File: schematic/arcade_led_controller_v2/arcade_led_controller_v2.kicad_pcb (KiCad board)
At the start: 2 copper layers, 104.1 x 70 mm, 930 parts, among them P1_BALLTOP_LED_1 WS2812B, P1_BUTTONS_LED1 WS2812B, P1_DP_JOY_MODE_LED1 LED, P1_JOYSTICK_LED1 WS2812B, P1_LS_JOY_MODE_LED1 LED, P1_RS_JOY_MODE_LED1 LED, P2_BALLTOP_LED_1 WS2812B, P2_BUTTONS_LED1 WS2812B, P2_DP_JOY_MODE_LED1 LED, P2_JOYSTICK_LED1 WS2812B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

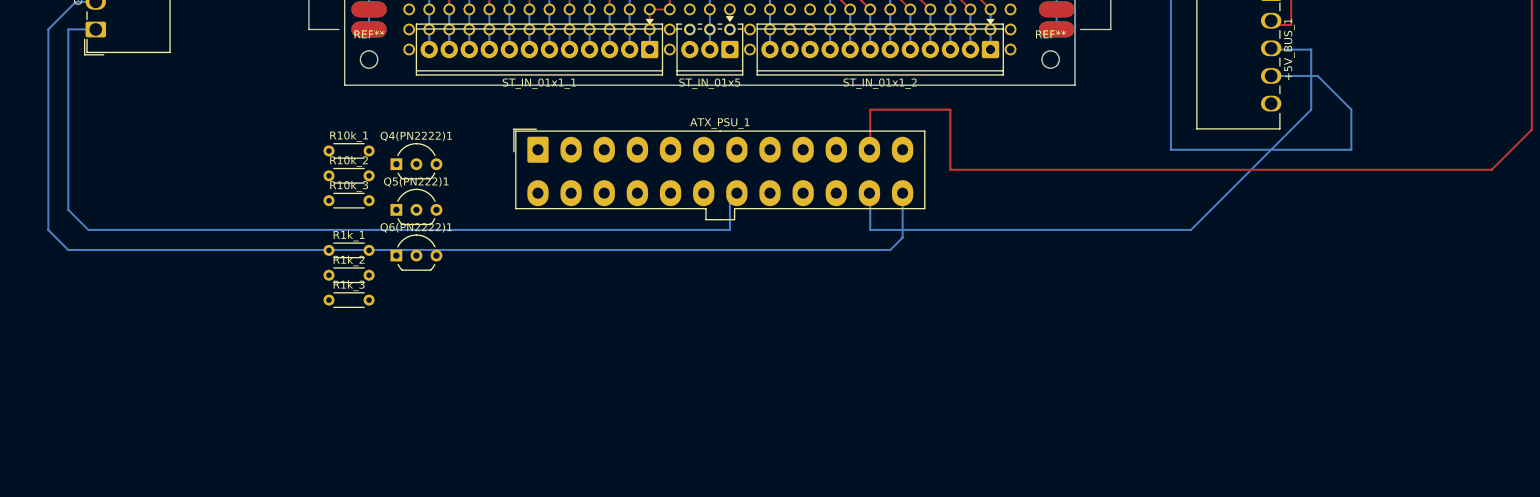
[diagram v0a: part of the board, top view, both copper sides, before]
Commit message: Update input pin assignments
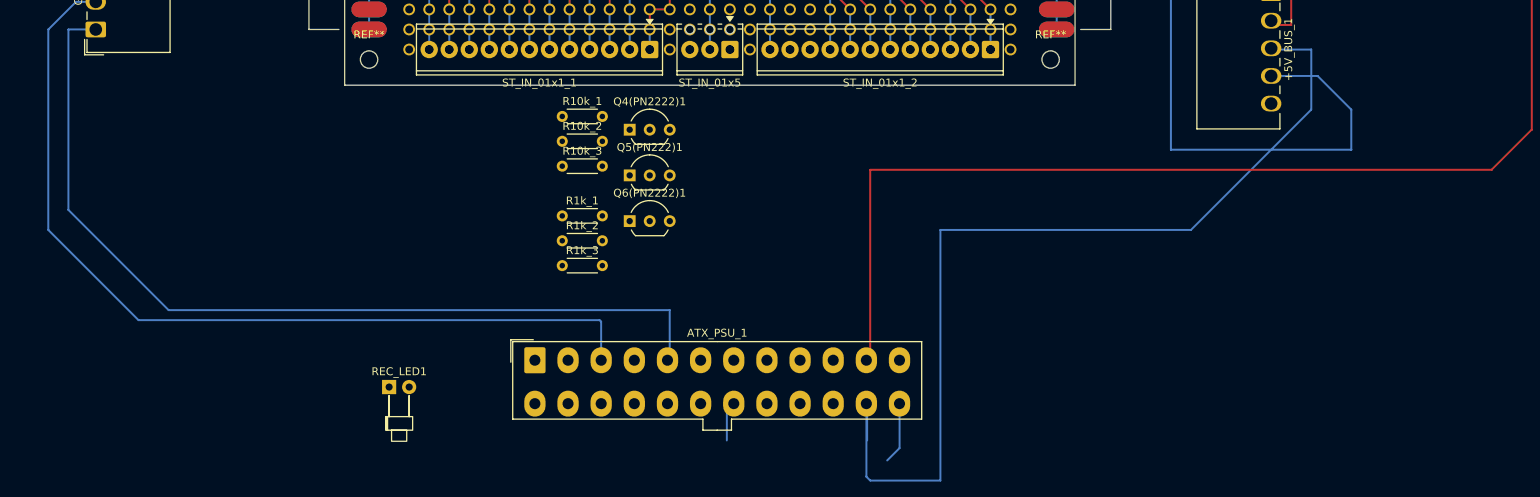
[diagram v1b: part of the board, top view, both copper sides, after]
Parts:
- added REC_LED1: LED, LED_THT:LED_D1.8mm_W1.8mm_H2.4mm_Horizontal_O3.81mm_Z1.6mm, F.Cu at (111.8, 174.8)
- moved Q4(PN2222)1 29.9 mm to (142.2, 142.2)
- moved Q5(PN222)1 29.9 mm to (142.2, 148.0)
- moved Q6(PN2222)1 29.9 mm to (142.2, 153.8)
- moved R10k_1 29.9 mm to (133.7, 140.6)
- moved R10k_2 29.9 mm to (133.7, 143.7)
- moved R1k_1 29.9 mm to (133.7, 153.2)
- moved R1k_2 29.9 mm to (133.7, 156.3)
- moved R1k_3 29.9 mm to (133.7, 159.5)
- moved R10k_3 29.9 mm to (133.7, 146.9)
- moved ATX_PSU_1 26.7 mm to (130.2, 171.4)
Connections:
- net /REC_LED renamed /REC_LED_CATHODE
- net Net-(Q4(PN2222)1-B) renamed /P2_LS_BASE_TO_GP
- net Net-(Q7(PN2222)1-B) renamed /REC_LED_BASE_TO_GP
- A1 pad 15: /ROTARY_SW -> Net-(A1-GPIO11)
- A1 pad 16: /ROTARY_DT -> /ROTARY_SW
- A1 pad 17: /P1_SIG -> /ROTARY_DT
- A1 pad 2: /P2_SIG -> /P1_SIG
- A1 pad 7: Net-(A1-GPIO5) -> /P2_SIG
- Q5(PN222)1 pad 2: Net-(Q5(PN222)1-B) -> GND
- Q6(PN2222)1 pad 2: Net-(Q6(PN2222)1-B) -> /P2_RS_BASE_TO_GP
- R10k_2 pad 1: Net-(Q5(PN222)1-B) -> GND
- R10k_3 pad 1: GND -> /P2_RS_BASE_TO_GP
- R10k_3 pad 2: Net-(Q6(PN2222)1-B) -> GND
- R1k_1 pad 1: Net-(A1-GPIO6) -> Net-(A1-GPIO8)
- R1k_2 pad 1: Net-(A1-GPIO8) -> Net-(A1-GPIO10)
- R1k_2 pad 2: Net-(Q5(PN222)1-B) -> GND
- R1k_3 pad 1: Net-(A1-GPIO10) -> Net-(A1-GPIO11)
- R1k_3 pad 2: Net-(Q6(PN2222)1-B) -> /P2_RS_BASE_TO_GP
- R1k_4 pad 1: Net-(A1-GPIO5) -> Net-(A1-GPIO6)
- ST_IN_01x1_1 pad 2: GND -> /P2_SIG
- ST_IN_01x1_1 pad 9: /P2_SIG -> /P1_SIG
- ST_IN_01x1_2 pad 10: unconnected-(ST_IN_01x1_2-Pin_10-Pad10) -> /P2_DP_CATHODE
- ST_IN_01x1_2 pad 11: /P2_DP_CATHODE -> unconnected-(ST_IN_01x1_2-Pin_11-Pad11)
- ST_IN_01x1_2 pad 4: /P1_SIG -> /ROTARY_DT
- ST_IN_01x1_2 pad 5: /ROTARY_DT -> /ROTARY_SW
- ST_IN_01x1_2 pad 7: /ROTARY_SW -> /P2_RS_CATHODE
- ST_IN_01x1_2 pad 8: /P2_RS_CATHODE -> unconnected-(ST_IN_01x1_2-Pin_8-Pad8)
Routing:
- net +5V: track 1173.2 -> 1214.9 mm
- net GND: track 2125.3 -> 2100.3 mm
- net /REC_LED_CATHODE: track 12.7 -> 0.00 mm
- net (no net): track 312.0 -> 324.7 mm
- net +12V: track 234.1 -> 245.7 mm

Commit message: update net classes
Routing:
- net (no net): track 324.7 -> 322.2 mm
- net Net-(A1-GPIO6): vias 1 -> 0
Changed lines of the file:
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@@
 		(capping no)
 		(filling no)
+		(zone_defaults)
 		(pcbplotparams
 			(layerselection 0x00000000_00000000_55555555_5755f5ff)
@@
 	)
 	(segment
-		(start 142.24 121.92)
-		(end 142.24 124.46)
-		(width 0.25)
-		(layer "B.Cu")
-		(net "")
-	)
-	(segment
 		(start 139.7 114.3)
 		(end 139.7 111.76)
@@
 	)
 	(via
+		(at 144.78 129.54)
+		(size 0.6)
+		(drill 0.4)
+		(layers "F.Cu" "B.Cu")
+		(capping no)
+		(covering
+			(front no)
+			(back no)
+		)
+		(plugging
+			(front no)
+			(back no)
+		)
+		(filling no)
+		(net "/REC_LED_CATHODE")
+	)
+	(via
+		(at 147.32 121.92)
+		(size 0.6)
+		(drill 0.4)
+		(layers "F.Cu" "B.Cu")
+		(capping no)
+		(covering
+			(front no)
+			(back no)
+		)
+		(plugging
+			(front no)
+			(back no)
+		)
+		(filling no)
+		(net "/REC_LED_CATHODE")
+	)
+	(via
 		(at 162.56 73.66)
 		(size 0.6)
@@
 	)
 	(via
-		(at 139.7 114.3)
-		(size 0.6)
-		(drill 0.4)
-		(layers "F.Cu" "B.Cu")
-		(capping no)
-		(covering
-			(front no)
-			(back no)
-		)
-		(plugging
-			(front no)
-			(back no)
-		)
-		(filling no)
-		(net "/DISPLAY_DC")
-	)
-	(via
-		(at 139.7 127)
+		(at 127 114.3)
 		(size 0.6)
 		(drill 0.4)
@@
 		)
 		(filling no)
-		(net "/DISPLAY_DC")
+		(net "/P2_SIG")
 	)
 	(via
-		(at 134.62 114.3)
+		(at 119.38 127)
 		(size 0.6)
 		(drill 0.4)
@@
 		)
 		(filling no)
-		(net "/DISPLAY_MOSI")
+		(net "/P2_SIG")
 	)
 	(via
-		(at 129.54 127)
+		(at 139.7 114.3)
 		(size 0.6)
 		(drill 0.4)
@@
 		)
 		(filling no)
-		(net "/DISPLAY_MOSI")
+		(net "/DISPLAY_DC")
 	)
 	(via
-		(at 129.54 114.3)
+		(at 139.7 127)
 		(size 0.6)
 		(drill 0.4)
@@
 		)
 		(filling no)
-		(net "/DISPLAY_SCK")
+		(net "/DISPLAY_DC")
 	)
 	(via
-		(at 124.46 127)
+		(at 134.62 114.3)
 		(size 0.6)
 		(drill 0.4)
@@
 		)
 		(filling no)
-		(net "/DISPLAY_SCK")
+		(net "/DISPLAY_MOSI")
 	)
 	(via
-		(at 127 114.3)
+		(at 129.54 127)
 		(size 0.6)
 		(drill 0.4)
@@
 		)
 		(filling no)
-		(net "/P2_SIG")
+		(net "/DISPLAY_MOSI")
 	)
 	(via
-		(at 119.38 127)
+		(at 129.54 114.3)
 		(size 0.6)
 		(drill 0.4)
@@
 		)
 		(filling no)
-		(net "/P2_SIG")
+		(net "/DISPLAY_SCK")
 	)
 	(via
-		(at 147.32 114.3)
+		(at 124.46 127)
 		(size 0.6)
 		(drill 0.4)
@@
 		)
 		(filling no)
-		(net "Net-(A1-GPIO6)")
+		(net "/DISPLAY_SCK")
 	)
 	(via
@@
 		(net "/2Y(2)")
 	)
-	(via
-		(at 144.78 129.54)
-		(size 0.6)
-		(drill 0.4)
-		(layers "F.Cu" "B.Cu")
-		(capping no)
-		(covering
-			(front no)
-			(back no)
-		)
-		(plugging
-			(front no)
-			(back no)
-		)
-		(filling no)
-		(net "/REC_LED_CATHODE")
-	)
-	(via
-		(at 147.32 121.92)
-		(size 0.6)
-		(drill 0.4)
-		(layers "F.Cu" "B.Cu")
-		(capping no)
-		(covering
-			(front no)
-			(back no)
-		)
-		(plugging
-			(front no)
-			(back no)
-		)
-		(filling no)
-		(net "/REC_LED_CATHODE")
-	)
 	(embedded_fonts no)

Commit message: complete track routing
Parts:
- moved P2_DP_JOY_MODE_LED1 142.2 mm to (162.6, 143.5)
- moved P2_LS_JOY_MODE_LED1 142.1 mm to (152.4, 143.5)
- moved P2_RS_JOY_MODE_LED1 142.0 mm to (170.2, 143.5)
- moved U3 98.7 mm to (17.8, 139.3)
- moved P1_LS_JOY_MODE_LED1 59.5 mm to (154.9, 59.7), turned to 180 degrees
- moved P1_DP_JOY_MODE_LED1 59.2 mm to (147.3, 59.7), turned to 180 degrees
- moved P1_RS_JOY_MODE_LED1 58.9 mm to (138.4, 59.7), turned to 180 degrees
- moved R1k_3 52.9 mm to (165.1, 116.8)
- moved R1k_2 46.1 mm to (157.5, 116.8)
- moved R10k_3 45.7 mm to (170.2, 119.4)
- moved REC_LED1 43.7 mm to (142.2, 143.5)
- moved Q6(PN2222)1 40.8 mm to (167.6, 121.9)
- moved R1k_1 39.8 mm to (149.9, 116.8)
- moved R10k_2 37.7 mm to (162.6, 119.4)
- moved Q5(PN222)1 31.6 mm to (160.0, 121.9)
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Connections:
- net Net-(A1-GPIO11) renamed /RS_1K_TO_GP
- net Net-(A1-GPIO6) renamed /REC_1K_TO_GP
- A1 pad 10: unconnected-(A1-GPIO7-Pad10) -> /LS_1K_TO_GP
- A1 pad 11: Net-(A1-GPIO8) -> /DP_1K_TO_GP
- A1 pad 14: Net-(A1-GPIO10) -> unconnected-(A1-GPIO10-Pad14)
- Q5(PN222)1 pad 2: GND -> /P2_DP_BASE_TO_GP
- R10k_2 pad 1: GND -> /P2_DP_BASE_TO_GP
- R1k_1 pad 1: Net-(A1-GPIO8) -> /LS_1K_TO_GP
- R1k_2 pad 1: Net-(A1-GPIO10) -> /DP_1K_TO_GP
- R1k_2 pad 2: GND -> /P2_DP_BASE_TO_GP
- ST_IN_01x5 pad 1: unconnected-(ST_IN_01x5-Pin_1-Pad1) -> /P2_LS_CATHODE
- ST_IN_01x5 pad 3: /P2_LS_CATHODE -> unconnected-(ST_IN_01x5-Pin_3-Pad3)
- ST_OUT_01x12_2 pad 11: ROTARY_+5V -> unconnected-(ST_OUT_01x12_2-Pin_11-Pad11)
- ST_OUT_01x12_2 pad 12: DISPLAYT_+5V -> ROTARY_+5V
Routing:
- net (no net): track 322.2 -> 61.0 mm
- net /DISPLAY_RST: track 25.6 -> 176.2 mm, vias 4 -> 2
- net GND: track 2100.3 -> 2000.0 mm
- net +5V: track 1214.9 -> 1125.2 mm
- net /DISPLAY_CS: track 0.00 -> 83.5 mm
- net /1A: track 0.00 -> 43.4 mm, vias 0 -> 2
- net /ROTARY_SW: track 0.00 -> 27.1 mm
- net /ROTARY_DT: track 0.00 -> 25.6 mm
- net /ROTARY_CLK: track 0.00 -> 25.6 mm, vias 2 -> 3
- net /REC_LED_CATHODE: track 0.00 -> 25.0 mm
- net /P2_LS_CATHODE: track 0.00 -> 25.0 mm, vias 0 -> 2
- net /DISPLAY_SCK: track 0.00 -> 22.4 mm
- net /P1_SIG: track 0.00 -> 22.4 mm, vias 0 -> 2
- net /DISPLAY_MOSI: track 0.00 -> 21.4 mm
- net /P2_RS_CATHODE: track 0.00 -> 21.2 mm, vias 1 -> 2
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
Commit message: wrapping up v2 schematic and pcb changes. Update pins.h to match
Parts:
- removed GND_BUS_1, GND_BUS_2: Conn_01x05_Pin, Connector_Wago:Wago_734-165_1x05_P3.50mm_Horizontal
- added +12V_BUS_1: Conn_01x05_Pin, TerminalBlock_WAGO:TerminalBlock_WAGO_233-505_2x05_P2.54mm, F.Cu at (233.7, 165.0)
- added +12V_BUS_2: Conn_01x05_Pin, TerminalBlock_WAGO:TerminalBlock_WAGO_233-505_2x05_P2.54mm, F.Cu at (251.5, 165.1)
- added J1: GND_BUS_1, TerminalBlock_WAGO:TerminalBlock_WAGO_233-506_2x06_P2.54mm, F.Cu at (86.3, 97.8)
- added J2: GND_BUS_2, TerminalBlock_WAGO:TerminalBlock_WAGO_233-504_2x04_P2.54mm, F.Cu at (77.4, 77.5)
- added J3: PSU_GND_BUS, Connector_Wago:Wago_734-163_1x03_P3.50mm_Horizontal, F.Cu at (78.7, 129.5)
- moved P2_BALLTOP_LED_1 8.37 mm to (104.5, 63.0)
- moved P2_JOYSTICK_LED1 1.62 mm to (104.8, 57.9)
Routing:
- net +12V: track 245.7 -> 1416.2 mm
- net GND: track 2000.0 -> 1790.6 mm
- net +5V: track 1125.2 -> 1237.5 mm
- net /P2_BALLTOP_DATA: track 8.06 -> 0.00 mm
- net /P2_JOYSTICK_DATA: track 26.0 -> 24.4 mm
